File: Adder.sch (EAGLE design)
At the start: 57 parts, among them U1 LMS8117

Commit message: Made updates for v2
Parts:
- removed R19, R20, R21, R22: 51, SparkFun-Resistors:RESISTOR0805-RES
- removed R23, R24, R25, R26, R27, R28, R29, R30, R31: 10K, SparkFun-Resistors:RESISTOR0805-RES
- removed U$2, U$3, U$4, U$5, U$6: N-CHANNEL-MOSFET-BSS138, GeekAmmo:N-CHANNEL-MOSFET-BSS138
- added Q1, Q2, Q3, Q4, Q5: BSS101, transistor-fet:BSS101
- R10, R11, R12, R13, R14, R15, R16, R17, R18: value 51 -> 10K
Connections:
- removed net N$11: R1.1, S0.A
- removed net N$12: R2.1, S1.A
- removed net N$13: R3.1, S2.A
- removed net N$14: R4.1, S3.A
- removed net N$15: COUT.A, R5.1
- removed net N$24: A0.A, R13.1
- removed net N$25: A1.A, R12.1
- removed net N$26: A2.A, R11.1
- removed net N$27: A3.A, R10.1
- removed net N$28: B0.A, R9.1
- removed net N$29: B1.A, R8.1
- removed net N$30: B2.A, R7.1
- removed net N$31: B3.A, R6.1
- net 3.3V: now also COUT.A, S0.A, S1.A, S2.A, S3.A; no longer R1.2, R2.2, R3.2, R4.2, R5.2
- net A0_IN: now also A0.A, R1.2, R10.2; no longer R13.2, R14.2, R23.2
- net A1_IN: now also A1.A, R3.2; no longer R16.2, R25.2
- net A2_IN: now also A2.A, R14.2, R5.2; no longer R11.2, R18.2, R27.2
- net A3_IN: now also A3.A, R16.2, R7.2; no longer R10.2, R20.2, R29.2
- net B0_IN: now also B0.A, R11.2, R2.2; no longer R15.2, R24.2, R9.2
- net B1_IN: now also B1.A, R13.2, R4.2; no longer R17.2, R26.2, R8.2
- net B2_IN: now also B2.A, R15.2, R6.2; no longer R19.2, R28.2, R7.2
- net B3_IN: now also B3.A, R17.2, R8.2; no longer R21.2, R30.2, R6.2
- net CIN: now also R9.2; no longer R22.2
- net COUT: now also Q5.G; no longer U$6.G
- net GND: now also Q1.S, Q2.S, Q3.S, Q4.S, Q5.S, R10.1, R11.1, R12.1, R13.1, R14.1, R15.1, R16.1, R17.1, R18.2; no longer R23.1, R24.1, R25.1, R26.1, R27.1, R28.1, R29.1, R30.1, R31.2, U$2.S, U$3.S, U$4.S, U$5.S, U$6.S
- net N$1: now also Q2.G; no longer U$3.G
- net N$10: now also Q5.D; no longer U$6.D
- net N$2: now also Q3.G; no longer U$4.G
- net N$3: now also Q4.G; no longer U$5.G
- net N$32: now also R1.1; no longer R14.1
- net N$33: now also R2.1; no longer R15.1
- net N$34: now also R3.1; no longer R16.1
- net N$35: now also R4.1; no longer R17.1
- net N$36: now also R5.1; no longer R18.1
- net N$37: now also R6.1; no longer R19.1
- net N$38: now also R7.1; no longer R20.1
- net N$39: now also R8.1; no longer R21.1
- net N$4: now also Q1.G; no longer U$2.G
- net N$40: now also R18.1, R9.1; no longer R22.1, R31.1
- net N$6: now also Q1.D; no longer U$2.D
- net N$7: now also Q2.D; no longer U$3.D
- net N$8: now also Q3.D; no longer U$4.D
- net N$9: now also Q4.D; no longer U$5.D
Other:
- moved on the sheet: COUT, R1, R10, R11, R12, R13, R14, R15, R16, R17, R18, R2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

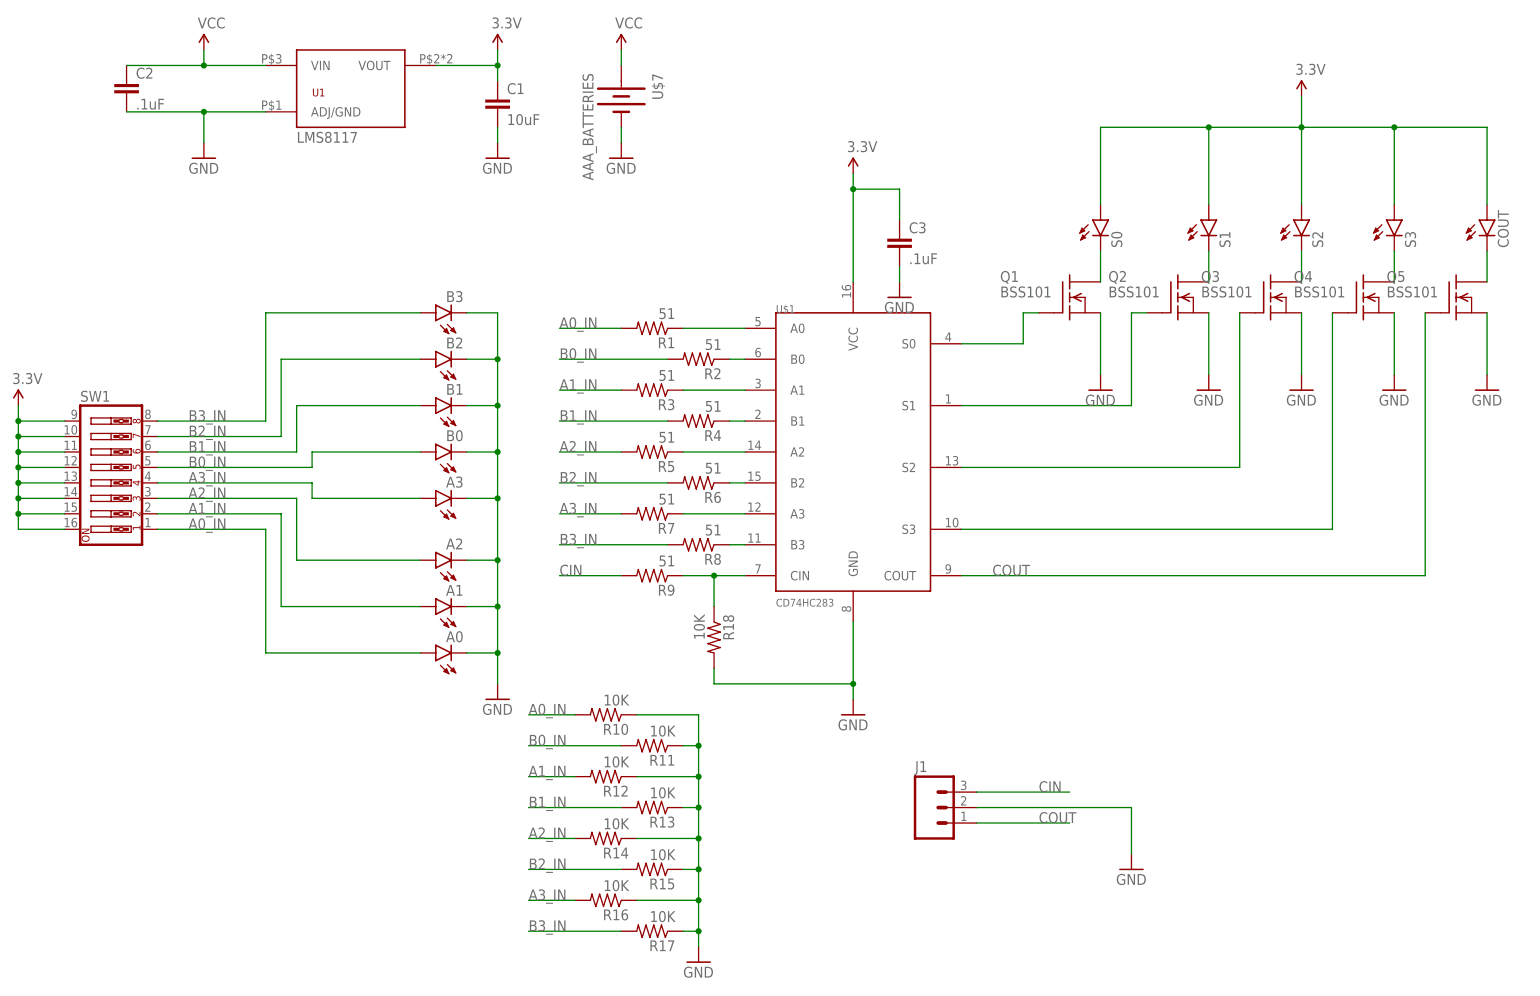
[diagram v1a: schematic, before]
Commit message: Finished updating v2 of board
Addressed comments in readme and refined layout
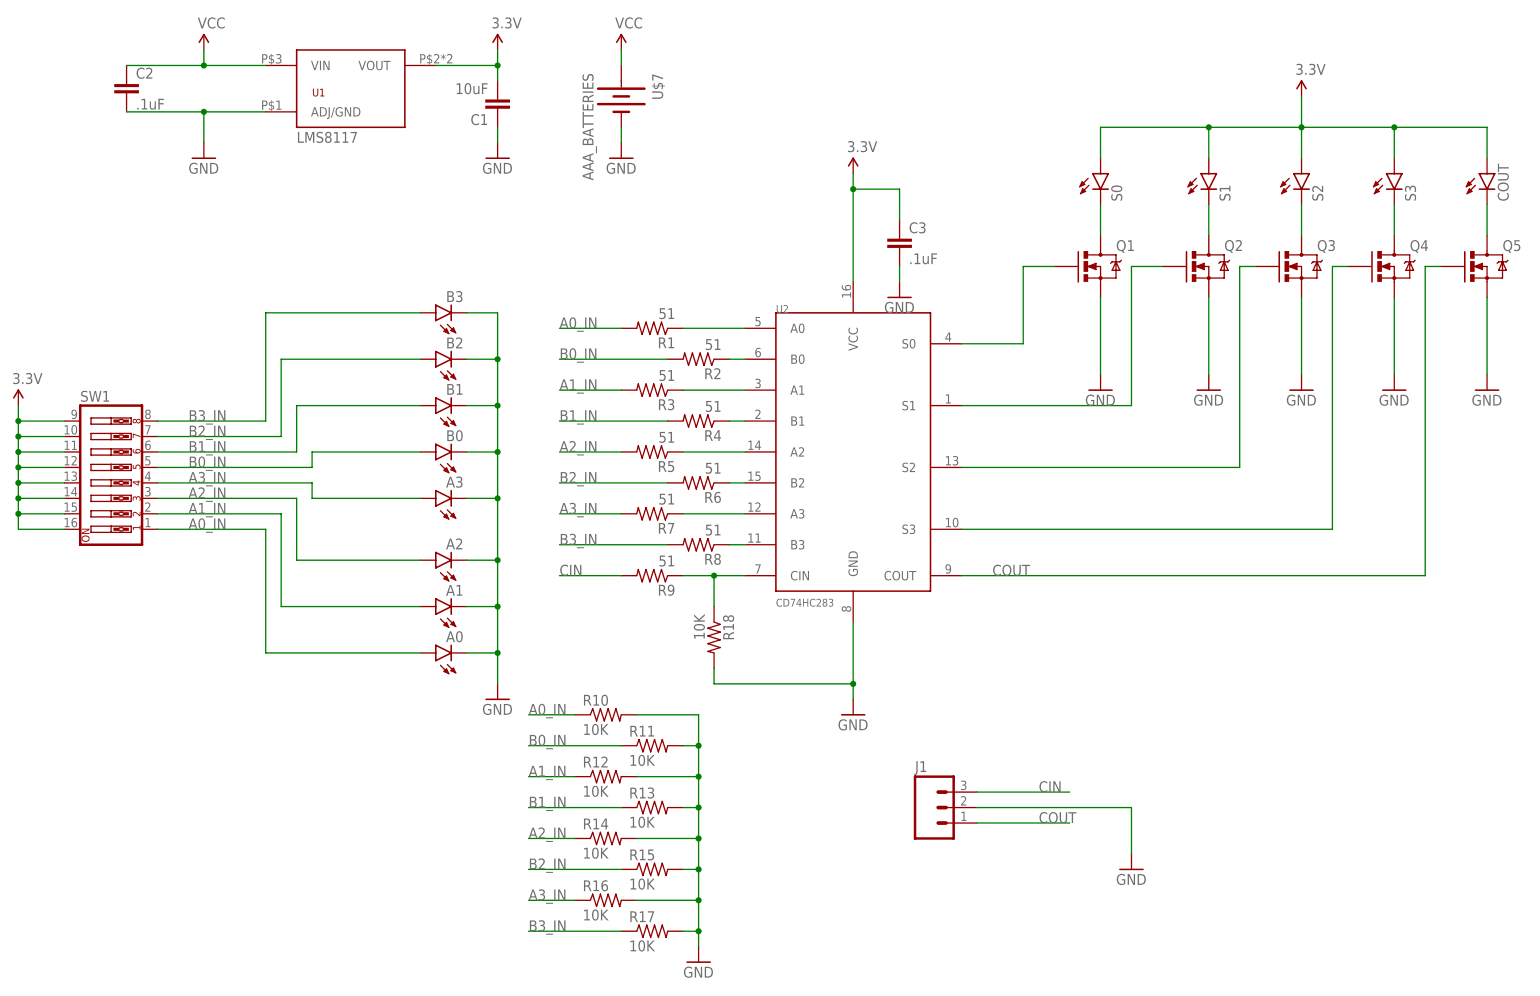
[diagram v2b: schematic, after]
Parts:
- Q1, Q2, Q3, Q4, Q5: value BSS101 -> MOSFET-NCHANNEL2N7000; device transistor-fet:BSS101 -> SparkFun-DiscreteSemi:MOSFET-NCHANNEL2N7000
- renumbered U$1 to U2
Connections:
- net 3.3V: now also C1.2; no longer C1.1
- net A0_IN: now also R10.1; no longer R10.2
- net A1_IN: now also R12.1; no longer R12.2
- net A2_IN: now also R14.1; no longer R14.2
- net A3_IN: now also R16.1; no longer R16.2
- net B0_IN: now also R11.1; no longer R11.2
- net B1_IN: now also R13.1; no longer R13.2
- net B2_IN: now also R15.1; no longer R15.2
- net B3_IN: now also R17.1; no longer R17.2
- net GND: now also C1.1, R10.2, R11.2, R12.2, R13.2, R14.2, R15.2, R16.2, R17.2; no longer C1.2, R10.1, R11.1, R12.1, R13.1, R14.1, R15.1, R16.1, R17.1
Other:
- moved on the sheet: C1, COUT, R10, R11, R12, R13, R14, R15, R16, R17, S0, S1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
